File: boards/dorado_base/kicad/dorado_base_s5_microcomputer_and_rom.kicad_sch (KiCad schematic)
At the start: 11 parts

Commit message: kicad export: emit Footprint property mapped from librarian package
Adds PACKAGE_TO_KICAD_FP table mapping librarian `package` strings
("DIP-14", "DIP-40", …) to KiCad stock footprint ids ("Package_DIP:
DIP-14_W7.62mm", "Package_DIP:DIP-40_W15.24mm", …). The table covers
every package currently in chips.json. Width convention: ≤20 pins →
0.3" (W7.62mm), ≥24 pins → 0.6" (W15.24mm), which matches the actual
chips in our librarian (≥24-pin parts are all memory/CPU, always 0.6"-
wide DIPs). Parts can override with an explicit `kicad_footprint`
field if a future chip breaks the rule.

Both lib_symbols and instance properties carry the footprint, so
`kicad-cli sch export bom` reports the correct land pattern per refdes.
No PCB-side library config needed — Package_DIP ships with KiCad.

Verified on dorado_base sheet 5 (still ERC PASS) and exidy_440 sheet 1
(blocking=0 unchanged); BOMs show every component mapped correctly.

Co-Authored-By: Claude Opus 4.7 (1M context) <noreply@anthropic.com>
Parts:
- b61, c61, h61, i61: footprint (none) -> Package_DIP:DIP-24_W15.24mm
- c07, d08, e07, g11: footprint (none) -> Package_DIP:DIP-16_W7.62mm
- c08, g08: footprint (none) -> Package_DIP:DIP-14_W7.62mm
- f61: footprint (none) -> Package_DIP:DIP-40_W15.24mm
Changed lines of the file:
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@@
     (property "Value" "MC12061" (at 69.85 90.74 0)
       (effects (font (size 1.27 1.27))))
-    (property "Footprint" "" (at 69.85 78.74 0)
+    (property "Footprint" "Package_DIP:DIP-16_W7.62mm" (at 69.85 78.74 0)
       (effects (font (size 1.27 1.27)) (hide yes)))
     (property "Datasheet" "" (at 69.85 78.74 0)
@@
     (property "Value" "74LS74" (at 140.97 52.64 0)
       (effects (font (size 1.27 1.27))))
-    (property "Footprint" "" (at 140.97 40.64 0)
+    (property "Footprint" "Package_DIP:DIP-14_W7.62mm" (at 140.97 40.64 0)
       (effects (font (size 1.27 1.27)) (hide yes)))
     (property "Datasheet" "" (at 140.97 40.64 0)
@@
     (property "Value" "74LS04" (at 106.68 102.17 0)
       (effects (font (size 1.27 1.27))))
-    (property "Footprint" "" (at 106.68 90.17 0)
+    (property "Footprint" "Package_DIP:DIP-14_W7.62mm" (at 106.68 90.17 0)
       (effects (font (size 1.27 1.27)) (hide yes)))
     (property "Datasheet" "" (at 106.68 90.17 0)
@@
     (property "Value" "2716" (at 187.96 85.66 0)
       (effects (font (size 1.27 1.27))))
-    (property "Footprint" "" (at 187.96 73.66 0)
+    (property "Footprint" "Package_DIP:DIP-24_W15.24mm" (at 187.96 73.66 0)
       (effects (font (size 1.27 1.27)) (hide yes)))
     (property "Datasheet" "" (at 187.96 73.66 0)
@@
     (property "Value" "JUMPER_PLUG_16" (at 107.95 145.35 0)
       (effects (font (size 1.27 1.27))))
-    (property "Footprint" "" (at 107.95 133.35 0)
+    (property "Footprint" "Package_DIP:DIP-16_W7.62mm" (at 107.95 133.35 0)
       (effects (font (size 1.27 1.27)) (hide yes)))
     (property "Datasheet" "" (at 107.95 133.35 0)
@@
     (property "Value" "2716" (at 187.96 139 0)
       (effects (font (size 1.27 1.27))))
-    (property "Footprint" "" (at 187.96 127 0)
+    (property "Footprint" "Package_DIP:DIP-24_W15.24mm" (at 187.96 127 0)
       (effects (font (size 1.27 1.27)) (hide yes)))
     (property "Datasheet" "" (at 187.96 127 0)
@@
     (property "Value" "2716" (at 187.96 250.76 0)
       (effects (font (size 1.27 1.27))))
-    (property "Footprint" "" (at 187.96 238.76 0)
+    (property "Footprint" "Package_DIP:DIP-24_W15.24mm" (at 187.96 238.76 0)
       (effects (font (size 1.27 1.27)) (hide yes)))
     (property "Datasheet" "" (at 187.96 238.76 0)
@@
     (property "Value" "2716" (at 187.96 202.5 0)
       (effects (font (size 1.27 1.27))))
-    (property "Footprint" "" (at 187.96 190.5 0)
+    (property "Footprint" "Package_DIP:DIP-24_W15.24mm" (at 187.96 190.5 0)
       (effects (font (size 1.27 1.27)) (hide yes)))
     (property "Datasheet" "" (at 187.96 190.5 0)
@@
     (property "Value" "74LS163" (at 113.03 70.42 0)
       (effects (font (size 1.27 1.27))))
-    (property "Footprint" "" (at 113.03 58.42 0)
+    (property "Footprint" "Package_DIP:DIP-16_W7.62mm" (at 113.03 58.42 0)
       (effects (font (size 1.27 1.27)) (hide yes)))
     (property "Datasheet" "" (at 113.03 58.42 0)
@@
     (property "Value" "74LS138" (at 132.08 231.71 0)
       (effects (font (size 1.27 1.27))))
-    (property "Footprint" "" (at 132.08 219.71 0)
+    (property "Footprint" "Package_DIP:DIP-16_W7.62mm" (at 132.08 219.71 0)
       (effects (font (size 1.27 1.27)) (hide yes)))
     (property "Datasheet" "" (at 132.08 219.71 0)
@@
     (property "Value" "MCS6502" (at 69.85 208.85 0)
       (effects (font (size 1.27 1.27))))
-    (property "Footprint" "" (at 69.85 196.85 0)
+    (property "Footprint" "Package_DIP:DIP-40_W15.24mm" (at 69.85 196.85 0)
       (effects (font (size 1.27 1.27)) (hide yes)))
     (property "Datasheet" "" (at 69.85 196.85 0)

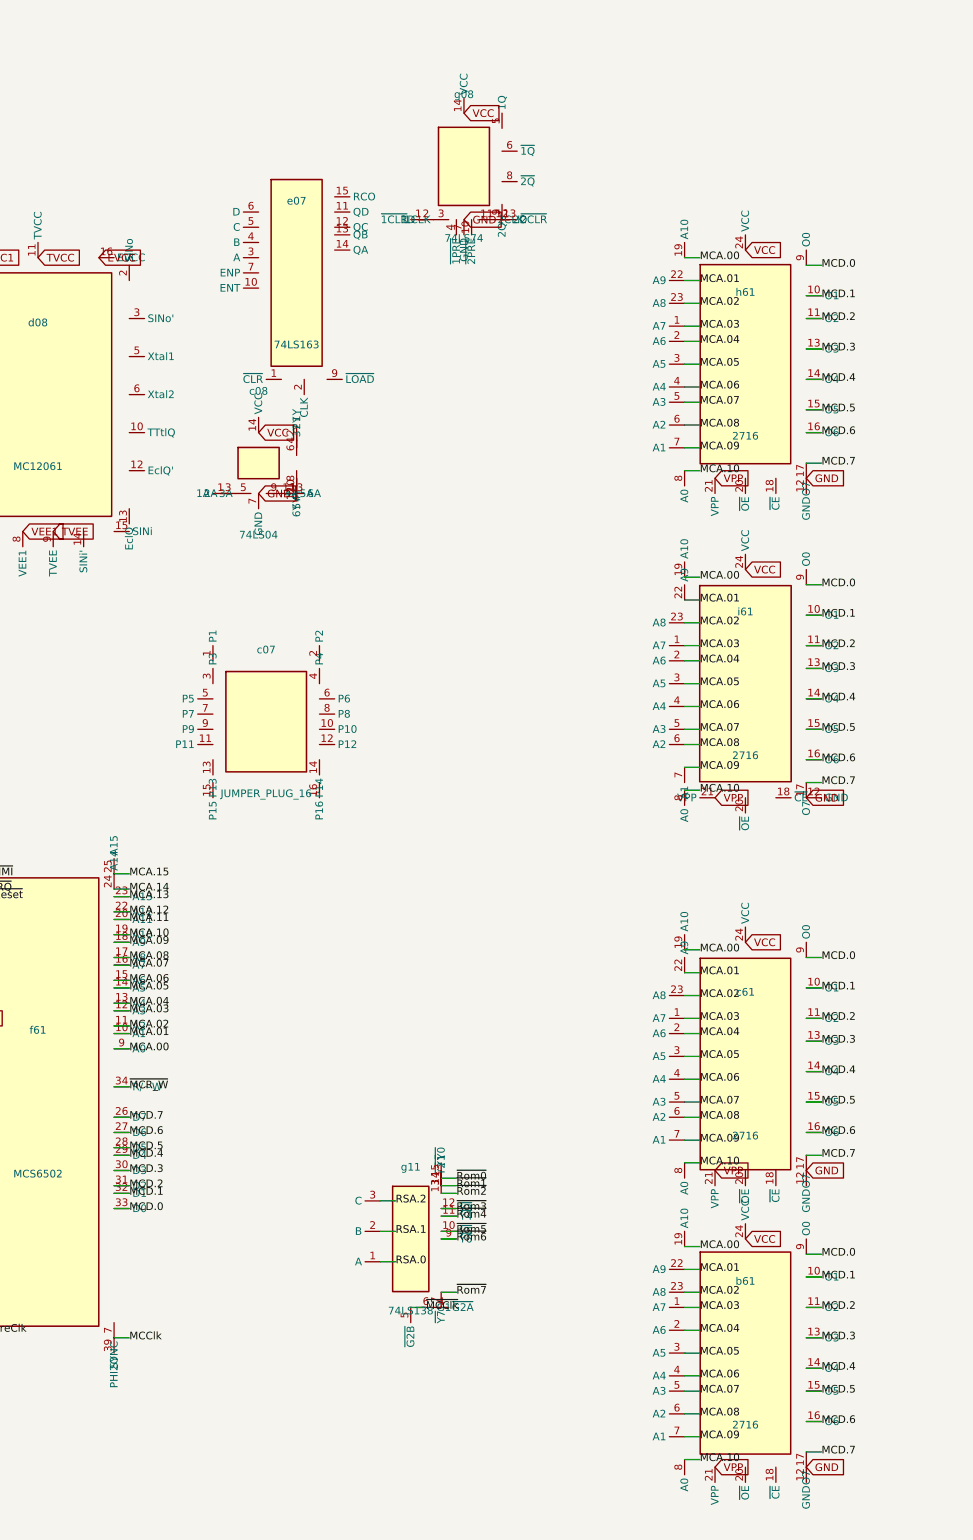
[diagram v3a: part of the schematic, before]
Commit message: kicad export: fix pin-tip / polyline snap mismatch (1.27 mm off-grid)
Two code paths emitted absolute mm coords differently:

  pin tip   = _snap(M + cx_px*s) + _snap((ix-cx_px)*s)      # double-snap
  polyline  = _snap(M + p[0]*s)                              # single-snap

`_snap(a) + _snap(b) != _snap(a+b)` in general — the difference is 0 or
±1 grid unit. On Z80 SBC, a hand-traced wire from J1.2 to U1.14 had its
endpoint at the polyline's snapped coord (71.12, 76.20) while the pin
tip lived at the double-snapped coord (72.39, 74.93). KiCad reported
wire_dangling and 8 other short wires had the same workaround applied
(converted to label nets to dodge it).

Fix:
- synth_faithful_symbol now derives lib-symbol pin coords from the
  absolute pin tip (single-snap) minus the instance origin, instead of
  snapping the local offset directly. The local pin offset is no longer
  guaranteed to be a whole grid unit — body and pin can drift up to
  ~0.6 mm relative to each other — but the absolute pin tip is now
  always on grid AND agrees with every other coord-emitting path.
- gen_sch's faithful branch uses the same single-snap formula for
  pin_endpoint_mm.

This makes pin tips, polyline points, junctions, and discrete pins all
share one snap convention. Validated on Z80 SBC: RS232_TX (a workaround
label) converted back to wire + path produces wire_dangling=0.

Regression: dorado_base sheets 5/7/8, z80_sbc sheet 1, exidy_440 sheet 1
all stay blocking=0. Pre-existing graph wiring errors (pin_to_pin,
multiple_net_names) unchanged.

Removes bugs/polyline-pin-snap-mismatch.md.

Co-Authored-By: Claude Opus 4.7 (1M context) <noreply@anthropic.com>
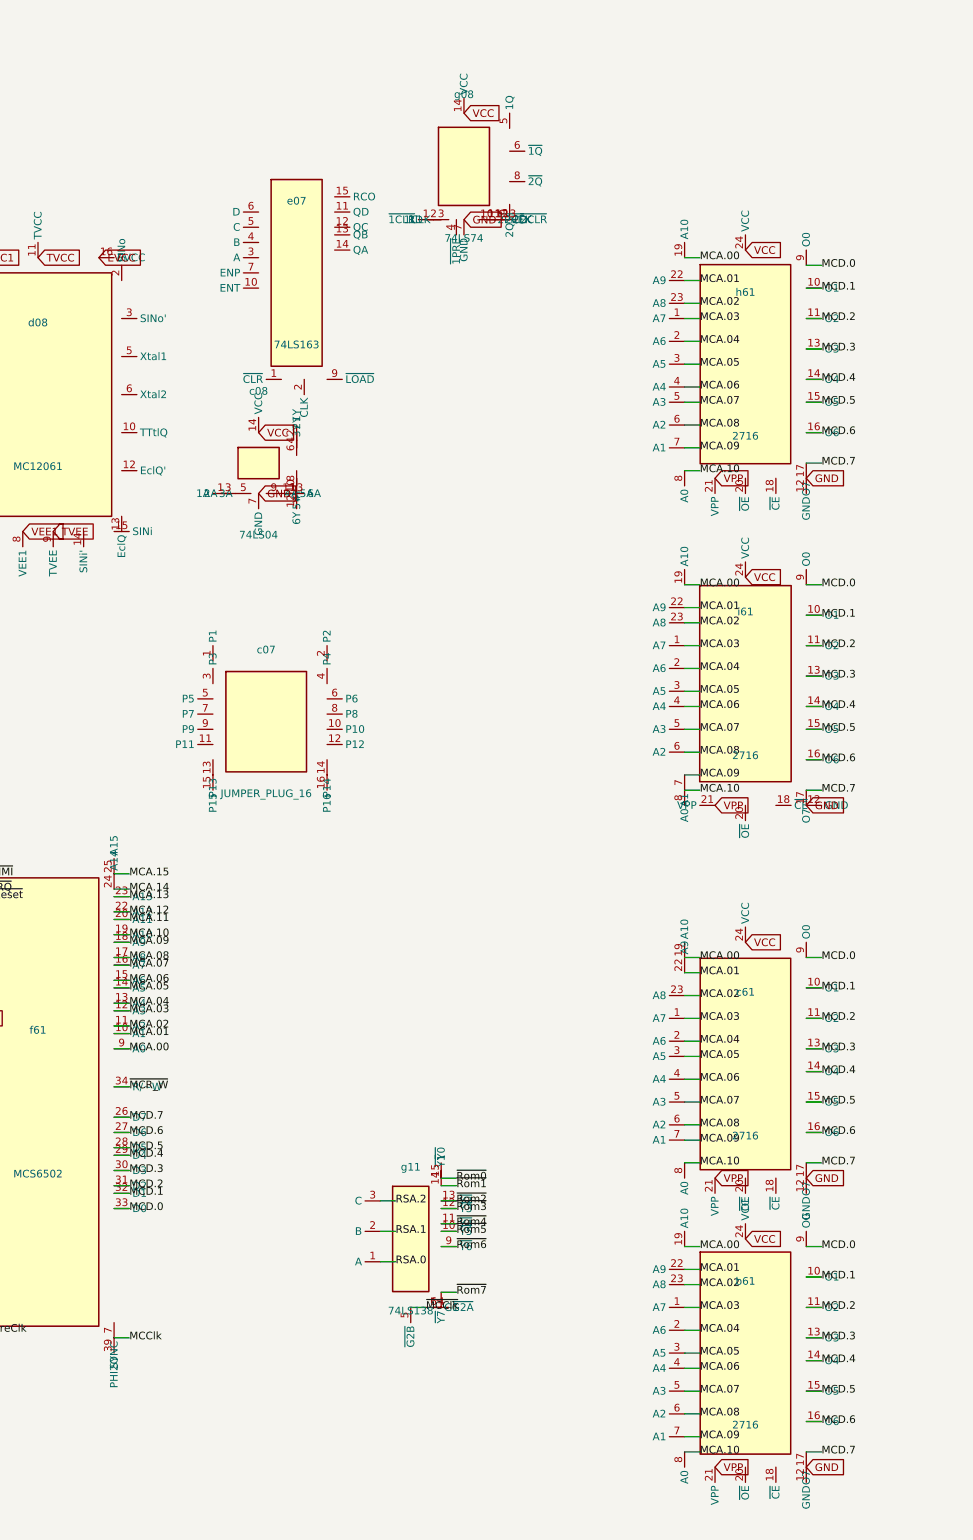
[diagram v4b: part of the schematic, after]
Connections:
- net ~{MCClk}: now also g11.6 (G1)
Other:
- moved on the sheet: c07, c61, d08, g08, i61
